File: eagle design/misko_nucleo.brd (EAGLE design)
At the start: 115 x 115 mm, 135 parts, among them IC1 ATMEGA1281-16AU, IC10 ORG1510-MK4, IC11 TPS3808G33DBVT, IC12 LTC4425, IC13 RN4678_BT_MODULE, IC14 ADXL345, IC15 74HCT1G32, IC16 FM25W256-SOIC, IC17 MICROSD_SPI_MODE, IC18 FH12-30S-0.5SH, IC19 DS1394U-33+, IC2 MC1525TT, IC23 SP3012-04UTG, IC3 TMP36GRTZ, IC4 TPS63031, IC5 MCP73871-2AAI/ML, IC6 MAX6818, IC7 FT230XS, IC8 SN74LVC1G3157DBVR - BT switch, IC9 SN74LVC1G3157DBVR - GPS switch, Q1 ABM3B-8MHZ-10-1-U-T, Q2 LFXTAL016178R, SW1 RESET, SW2 POWER SWITCH, SW3 MICROJOYSTICK, SW4 PB6156RSL, SW5 PB6156RSL, T1 BSS84

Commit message: - defined net classes, added power symbols, ground fill
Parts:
- moved IC5 86.2 mm to (170.7, 80.0)
- moved R13 86.2 mm to (174.5, 74.5)
- moved R27 86.2 mm to (128.1, 36.6)
- moved C1 86.2 mm to (183.8, 52.2)
- moved C10 86.2 mm to (92.2, 67.5)
- moved C11 86.2 mm to (152.5, 75.5)
- moved C12 86.2 mm to (136.0, 51.5)
- moved C13 86.2 mm to (181.5, 73.0)
- moved C14 86.2 mm to (94.2, 67.5)
- moved C15 86.2 mm to (98.2, 67.5)
- moved C16 86.2 mm to (107.8, 67.5)
- moved C17 86.2 mm to (107.8, 67.5)
- moved C18 86.2 mm to (169.2, 49.5)
- moved C19 86.2 mm to (171.5, 49.5)
- moved C2 86.2 mm to (180.5, 51.5)
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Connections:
- net N$13 renamed IOREF
- net N$14 renamed 3V3
- net N$15 renamed NRST
- net N$16 renamed BOOT0
- net N$18 renamed PF1
- net N$20 renamed PF0
- net N$21 renamed PD2
- net N$22 renamed PC15
- net N$23 renamed PC14
- net N$24 renamed PC13
- net N$25 renamed PC12
- net N$26 renamed PC11
- net N$27 renamed PC10
- net N$28 renamed PC3
- net N$29 renamed PC2
- net N$30 renamed PC1
- net N$32 renamed PC0
- net N$33 renamed PB0
- net N$34 renamed PA15
- net N$35 renamed PA14
- net N$36 renamed PA13
- net N$37 renamed PA2
- net N$38 renamed PA1
- net N$39 renamed PA0
- net N$40 renamed AVDD
- net N$41 renamed VBUS_STLK
- net N$42 renamed PC4
- net N$43 renamed PC5
- net N$44 renamed PC6
- net N$45 renamed PC7
- net N$46 renamed PC8
- net N$47 renamed PC9
- net N$5 renamed VBAT
- net N$50 renamed PA5
- net N$51 renamed PA6
- net N$52 renamed PA7
- net N$53 renamed PA9
- net N$54 renamed PA8
- net N$55 renamed PB1
- net N$56 renamed PB2
- net N$57 renamed PB4
- net N$58 renamed PB5
- net N$59 renamed PB6
- net N$60 renamed PB7
- net N$61 renamed PB8
- net N$62 renamed PB10
- net N$63 renamed PN12
- net N$64 renamed PB13
- net N$65 renamed PB14
- net N$66 renamed PB15
- net N$7 renamed VDD
- net N$8 renamed VIN
- net N$9 renamed E5V
- removed net N$12: MISKO.CN7_18
- removed net N$17: MISKO.CN7_19, MISKO.CN7_20, MISKO.CN7_22, MISKO.CN7_8
- removed net N$48: MISKO.CN10_32
- removed net N$49: MISKO.CN10_20, MISKO.CN10_9
- new net OLD_5V0: C42.2, D2.A, IC23.10, IC5.17_CE, IC5.18_IN1, IC5.19_IN2, IC5.3_SEL, IC5.4_PROG2, IC5.9_!TE!, IC7.12, R12.1
- net 5V0: now also MISKO.CN7_18; no longer C42.2, D2.A, IC23.10, IC5.17_CE, IC5.18_IN1, IC5.19_IN2, IC5.3_SEL, IC5.4_PROG2, IC5.9_!TE!, IC7.12, R12.1
- net GND: now also MISKO.CN10_20, MISKO.CN10_32, MISKO.CN10_9, MISKO.CN7_19, MISKO.CN7_20, MISKO.CN7_22, MISKO.CN7_8
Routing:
- net OLD_5V0: track 0.00 -> 57.7 mm, vias 0 -> 6
- net 5V0: track 57.7 -> 0.00 mm, vias 6 -> 0
- net GPS_RED_LED_PIN: track 60.6 -> 59.3 mm
- net N$6: track 106.6 -> 106.0 mm

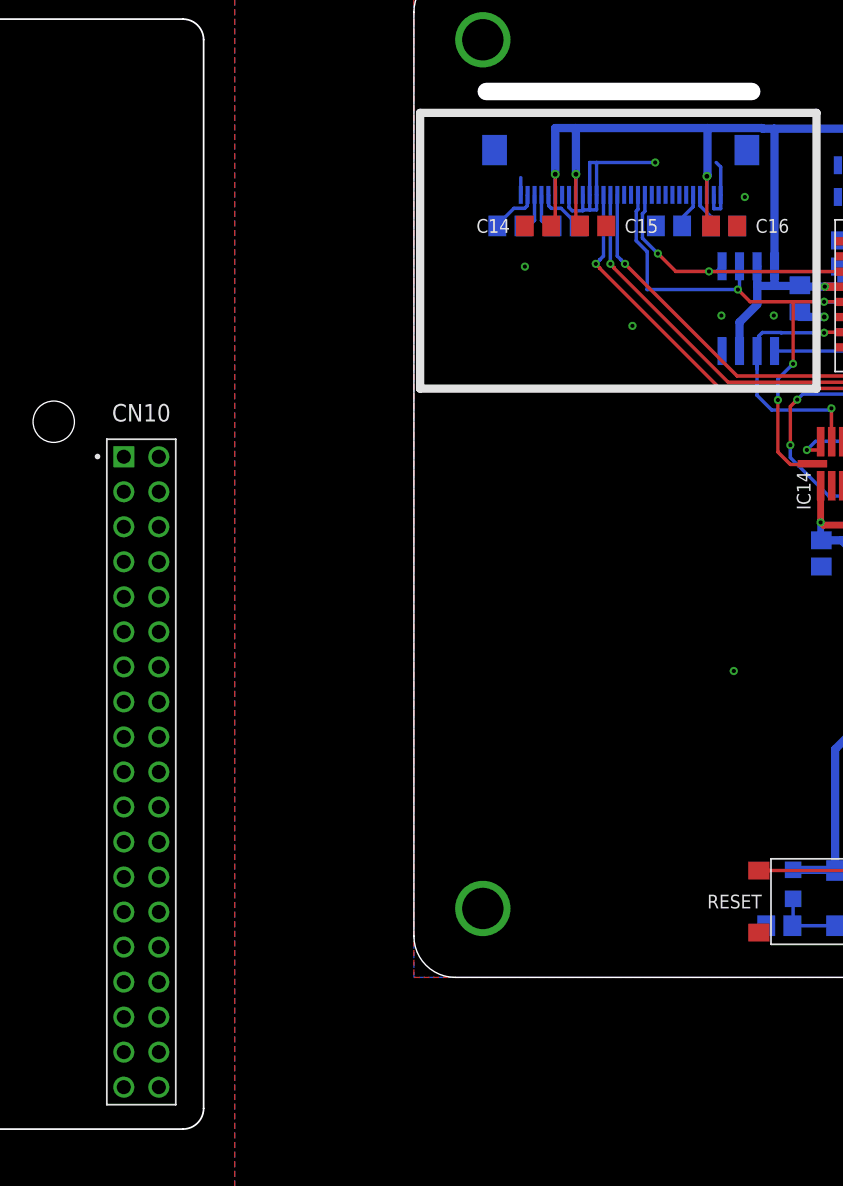
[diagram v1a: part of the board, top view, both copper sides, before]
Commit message: - annotated key peripherals to documentation layer - named nets for pin indentification
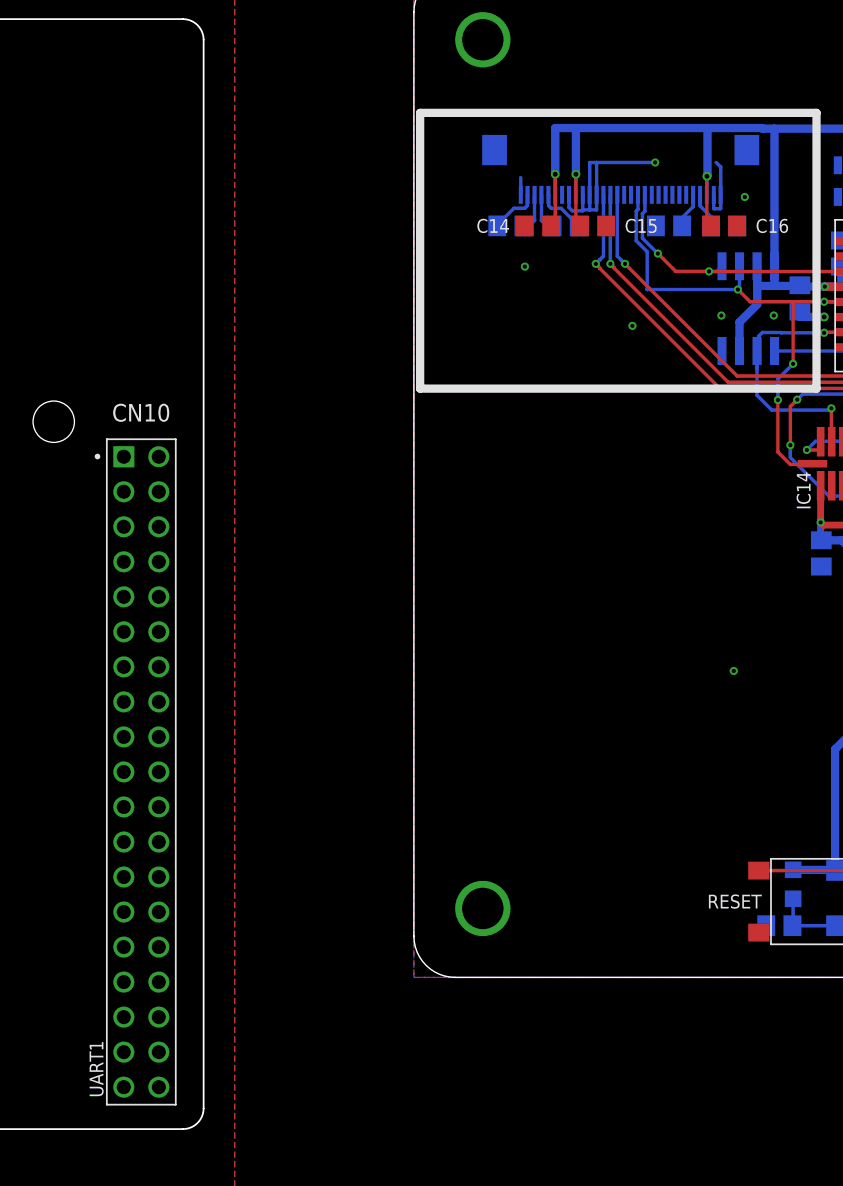
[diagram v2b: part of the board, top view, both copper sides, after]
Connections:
- net PA9 renamed PA10
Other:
- outline, holes or cut-outs redrawn
- board text added: "UART1"
- board text added: "can rx"
- board text added: "can tx"
- board text added: "lp uart1 rx"
- board text added: "lp uart1 tx"
- board text added: "lptim1 in1"
- board text added: "lptim1 in2"
- board text added: "lptim2 in1"
- board text added: "lptim2 in2"
- board text added: "misko POC ejovrh rev.3"
- board text added: "miso"
- board text added: "mosi"
- board text added: "sck"
- board text added: "uart2 rx"
- board text added: "uart2 tx"
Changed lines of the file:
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@@
 <setting verticaltext="up"/>
 </settings>
-<grid distance="0.25" unitdist="mm" unit="mm" style="lines" multiple="1" display="yes" altdistance="0.005" altunitdist="mm" altunit="mm"/>
+<grid distance="25" unitdist="mil" unit="mm" style="lines" multiple="1" display="yes" altdistance="0.005" altunitdist="mm" altunit="mm"/>
 <layers>
-<layer number="1" name="Top" color="4" fill="1" visible="yes" active="yes"/>
+<layer number="1" name="Top" color="4" fill="1" visible="no" active="yes"/>
 <layer number="2" name="Route2" color="1" fill="3" visible="no" active="no"/>
 <layer number="3" name="Route3" color="4" fill="3" visible="no" active="no"/>
@@
 <layer number="16" name="Bottom" color="1" fill="1" visible="no" active="yes"/>
 <layer number="17" name="Pads" color="2" fill="1" visible="yes" active="yes"/>
-<layer number="18" name="Vias" color="2" fill="1" visible="yes" active="yes"/>
+<layer number="18" name="Vias" color="2" fill="1" visible="no" active="yes"/>
 <layer number="19" name="Unrouted" color="6" fill="1" visible="yes" active="yes"/>
 <layer number="20" name="Dimension" color="14" fill="1" visible="yes" active="yes"/>
 <layer number="21" name="tPlace" color="7" fill="1" visible="yes" active="yes"/>
-<layer number="22" name="bPlace" color="7" fill="1" visible="no" active="yes"/>
+<layer number="22" name="bPlace" color="7" fill="1" visible="yes" active="yes"/>
 <layer number="23" name="tOrigins" color="15" fill="1" visible="yes" active="yes"/>
-<layer number="24" name="bOrigins" color="15" fill="1" visible="no" active="yes"/>
-<layer number="25" name="tNames" color="7" fill="1" visible="yes" active="yes"/>
+<layer number="24" name="bOrigins" color="15" fill="1" visible="yes" active="yes"/>
+<layer number="25" name="tNames" color="7" fill="1" visible="no" active="yes"/>
 <layer number="26" name="bNames" color="7" fill="1" visible="no" active="yes"/>
 <layer number="27" name="tValues" color="7" fill="1" visible="no" active="yes"/>
@@
 <layer number="38" name="bTest" color="7" fill="1" visible="no" active="yes"/>
 <layer number="39" name="tKeepout" color="4" fill="11" visible="yes" active="yes"/>
-<layer number="40" name="bKeepout" color="1" fill="11" visible="no" active="yes"/>
+<layer number="40" name="bKeepout" color="1" fill="11" visible="yes" active="yes"/>
 <layer number="41" name="tRestrict" color="4" fill="10" visible="yes" active="yes"/>
-<layer number="42" name="bRestrict" color="1" fill="10" visible="no" active="yes"/>
+<layer number="42" name="bRestrict" color="1" fill="10" visible="yes" active="yes"/>
 <layer number="43" name="vRestrict" color="2" fill="10" visible="yes" active="yes"/>
 <layer number="44" name="Drills" color="7" fill="1" visible="no" active="yes"/>
 <layer number="45" name="Holes" color="7" fill="1" visible="no" active="yes"/>
 <layer number="46" name="Milling" color="3" fill="1" visible="yes" active="yes"/>
-<layer number="47" name="Measures" color="7" fill="1" visible="no" active="yes"/>
-<layer number="48" name="Document" color="7" fill="1" visible="no" active="yes"/>
-<layer number="49" name="Reference" color="7" fill="1" visible="no" active="yes"/>
+<layer number="47" name="Measures" color="7" fill="1" visible="yes" active="yes"/>
+<layer number="48" name="Document" color="7" fill="1" visible="yes" active="yes"/>
+<layer number="49" name="Reference" color="7" fill="1" visible="yes" active="yes"/>
 <layer number="50" name="dxf" color="7" fill="1" visible="no" active="no"/>
 <layer number="51" name="tDocu" color="7" fill="1" visible="yes" active="yes"/>
-<layer number="52" name="bDocu" color="7" fill="1" visible="no" active="yes"/>
+<layer number="52" name="bDocu" color="7" fill="1" visible="yes" active="yes"/>
 <layer number="53" name="tGND_GNDA" color="7" fill="9" visible="no" active="no"/>
 <layer number="54" name="bGND_GNDA" color="1" fill="9" visible="no" active="no"/>
@@
 <wire x1="88.25" y1="13" x2="197.25" y2="13" width="0.1" layer="20"/>
 <wire x1="200.25" y1="16" x2="200.25" y2="84" width="0.1" layer="20"/>
-<dimension x1="85.25" y1="8" x2="200.25" y2="8" x3="142.75" y3="-9" textsize="1.778" layer="47" visible="yes"/>
-<dimension x1="80.25" y1="13" x2="80.25" y2="86" x3="73.25" y3="49.5" textsize="1.778" layer="47" visible="yes"/>
 <wire x1="198.25" y1="86" x2="88.25" y2="86" width="0.1" layer="20"/>
 <wire x1="85.25" y1="83" x2="85.25" y2="16" width="0.1" layer="20"/>
@@
 <wire x1="197.25" y1="128" x2="88.25" y2="128" width="0.1" layer="20"/>
 <wire x1="85.25" y1="125" x2="85.25" y2="111" width="0.1" layer="20"/>
-<wire x1="90.5" y1="77.25" x2="109.75" y2="77.25" width="1.27" layer="46"/>
 <wire x1="85.25" y1="83" x2="88.25" y2="86" width="0.1" layer="20" curve="-90"/>
 <wire x1="85.25" y1="16" x2="88.25" y2="13" width="0.1" layer="20" curve="90"/>
@@
 <text x="184.615" y="82.73" size="1.778" layer="21" font="vector" rot="R270" align="center">+</text>
 <text x="182.705" y="82.515" size="1.778" layer="21" font="vector" rot="R180" align="center">-</text>
+<text x="62.23" y="6.35" size="1" layer="21" rot="R90" align="center">UART1</text>
+<text x="60.96" y="25.4" size="1" layer="48" align="center">mosi</text>
+<text x="69.85" y="45.72" size="1" layer="48" align="center">sck</text>
+<text x="60.96" y="35.56" size="1" layer="48" align="center">miso</text>
+<text x="60.96" y="33.02" size="1" layer="48" align="center">mosi</text>
+<text x="8.89" y="5.08" size="1" layer="48" align="center">sck</text>
+<text x="0" y="7.62" size="1" layer="48" align="center">miso</text>
+<text x="0" y="5.08" size="1" layer="48" align="center">mosi</text>
+<text x="8.89" y="12.7" size="1" layer="48" align="center">sck</text>
+<text x="60.96" y="22.86" size="1" layer="48" align="center">sck</text>
+<text x="60.96" y="17.78" size="1" layer="48" align="center">miso</text>
+<text x="60.96" y="15.24" size="1" layer="48" align="center">mosi</text>
+<text x="60.325" y="45.72" size="1" layer="48" align="center">can tx</text>
+<text x="71.12" y="7.62" size="1" layer="48" align="center">can rx</text>
+<text x="60.325" y="48.26" size="1" layer="48" align="center">can tx</text>
+<text x="55.88" y="15.24" size="1" layer="48" align="center">can rx</text>
+<text x="55.88" y="17.78" size="1" layer="48" align="center">can tx</text>
+<text x="60.325" y="30.48" size="1" layer="48" align="center">can tx</text>
+<text x="71.12" y="50.8" size="1" layer="48" align="center">can rx</text>
+<text x="55.88" y="25.4" size="1" layer="48" align="center">can tx</text>
+<text x="59.69" y="27.94" size="1" layer="48" align="center">can rx</text>
+<text x="71.12" y="15.24" size="1" layer="48" align="center">can tx</text>
+<text x="15.875" y="12.7" size="1" layer="48" align="center">lp uart1 rx</text>
+<text x="10.795" y="10.16" size="1" layer="48" align="center">uart2 tx</text>
+<text x="71.755" y="22.86" size="1" layer="48" align="center">uart2 rx</text>
+<text x="55.245" y="22.86" size="1" layer="48" align="center">uart2 tx</text>
+<text x="52.705" y="27.94" size="1" layer="48" align="center">uart2 tx</text>
+<text x="48.895" y="25.4" size="1" layer="48" align="center">uart2 rx</text>
+<text x="57.785" y="10.16" size="1" layer="48" align="center">lp uart1 rx</text>
+<text x="48.895" y="15.24" size="1" layer="48" align="center">uart2 rx</text>
+<text x="52.705" y="48.26" size="1" layer="48" align="center">lp uart1 tx</text>
+<text x="52.705" y="45.72" size="1" layer="48" align="center">lp uart1 rx</text>
+<text x="9.525" y="17.78" size="1" layer="48" align="center">miso</text>
+<text x="16.51" y="17.78" size="1" layer="48" align="center">lptim1 in2</text>
+<text x="16.51" y="15.24" size="1" layer="48" align="center">lptim1 in1</text>
+<text x="25.4" y="12.7" size="1" layer="48" align="center">lptim1 in2</text>
+<text x="33.655" y="12.7" size="1" layer="48" align="center">uart2 tx</text>
+<text x="19.05" y="10.16" size="1" layer="48" align="center">lptim1 in1</text>
+<text x="80.645" y="22.86" size="1" layer="48" align="center">lptim1 in2</text>
+<text x="40.64" y="15.24" size="1" layer="48" align="center">lptim1 in1</text>
+<text x="11.43" y="7.62" size="1" layer="48" align="center">lptim2 in1</text>
+<text x="48.26" y="10.16" size="1" layer="48" align="center">lptim2 in2</text>
+<text x="58.42" y="20.32" size="1" layer="48" align="center">lptim2 in1</text>
+<text x="46.99" y="22.86" size="1" layer="48" align="center">lptim2 in1</text>
+<text x="12.7" y="73.66" size="1.5" layer="29" font="vector" ratio="12" align="center">misko POC
+ejovrh rev.3</text>
 </plain>
 <attributes>
@@
 <contactref element="MISKO" pad="CN10_15"/>
 </signal>
-<signal name="PA9" class="2">
+<signal name="PA10" class="2">
 <contactref element="MISKO" pad="CN10_33"/>
 </signal>

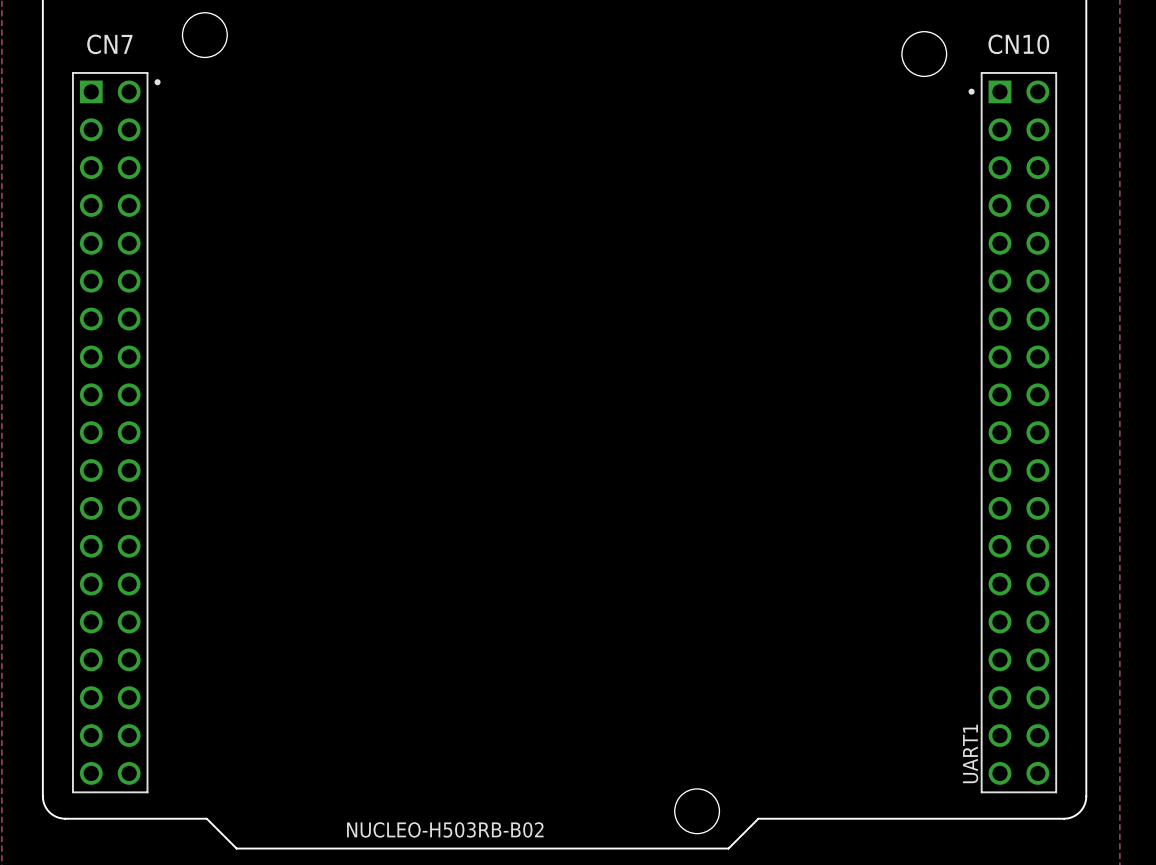
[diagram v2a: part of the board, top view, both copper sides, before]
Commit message: - defined and connected legacy board GPIOs
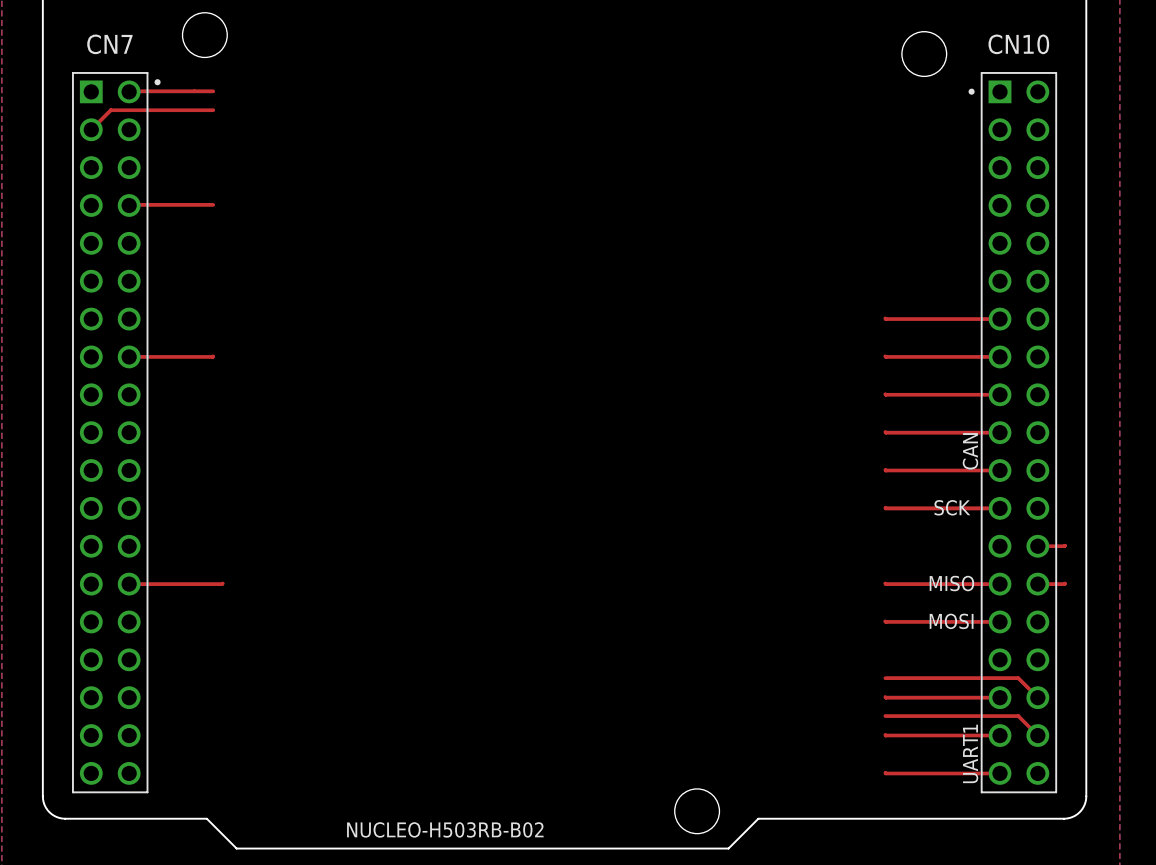
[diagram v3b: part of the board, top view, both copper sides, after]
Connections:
- net PA0 renamed ADC_VGPS
- net PA10 renamed GPS_WKUP
- net PA6 renamed SPI_FRAM_CS
- net PA7 renamed ADXL345_CS
- net PA8 renamed SPI1_SCK
- net PB14 renamed UART1_TX
- net PB15 renamed UART1_RX
- net PB4 renamed SPI1_MISO
- net PB5 renamed SPI1_MOSI
- net PB8 renamed ANAL_SW_CTRL
- net PC11 renamed GPS_GREEN_LED
- net PC12 renamed GPS_RED_LED
- net PC4 renamed GPS_PWR_CTRL
- net PC6 renamed CAN_RX
- net PC7 renamed CAN_TX
- net PC8 renamed DEBUG_OUT
- net PC9 renamed ADXL345_INT
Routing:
- net GPS_PWR_CTRL: track 0.00 -> 10.8 mm
- net ANAL_SW_CTRL: track 0.00 -> 10.8 mm
- net UART1_TX: track 0.00 -> 9.56 mm
- net UART1_RX: track 0.00 -> 9.56 mm
- net GPS_RED_LED: track 0.00 -> 8.72 mm
- net ADXL345_CS: track 0.00 -> 7.71 mm
- net SPI1_MISO: track 0.00 -> 7.71 mm
- net CAN_RX: track 0.00 -> 7.71 mm
- net SPI1_MOSI: track 0.00 -> 7.71 mm
- net GPS_WKUP: track 0.00 -> 7.71 mm
- net SPI_FRAM_CS: track 0.00 -> 7.71 mm
- net SPI1_SCK: track 0.00 -> 7.71 mm
- net CAN_TX: track 0.00 -> 7.71 mm
- net ADXL345_INT: track 0.00 -> 7.71 mm
- net ADC_VGPS: track 0.00 -> 6.29 mm
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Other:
- board text added: "CAN"
- board text added: "MISO"
- board text added: "MOSI"
- board text added: "SCK"
